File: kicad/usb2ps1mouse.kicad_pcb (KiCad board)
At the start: 2 copper layers, 42.7 x 35 mm, 11 parts, among them J1 Conn_01x09_Pin, J2 USB_A, U2 ME2108A50PG

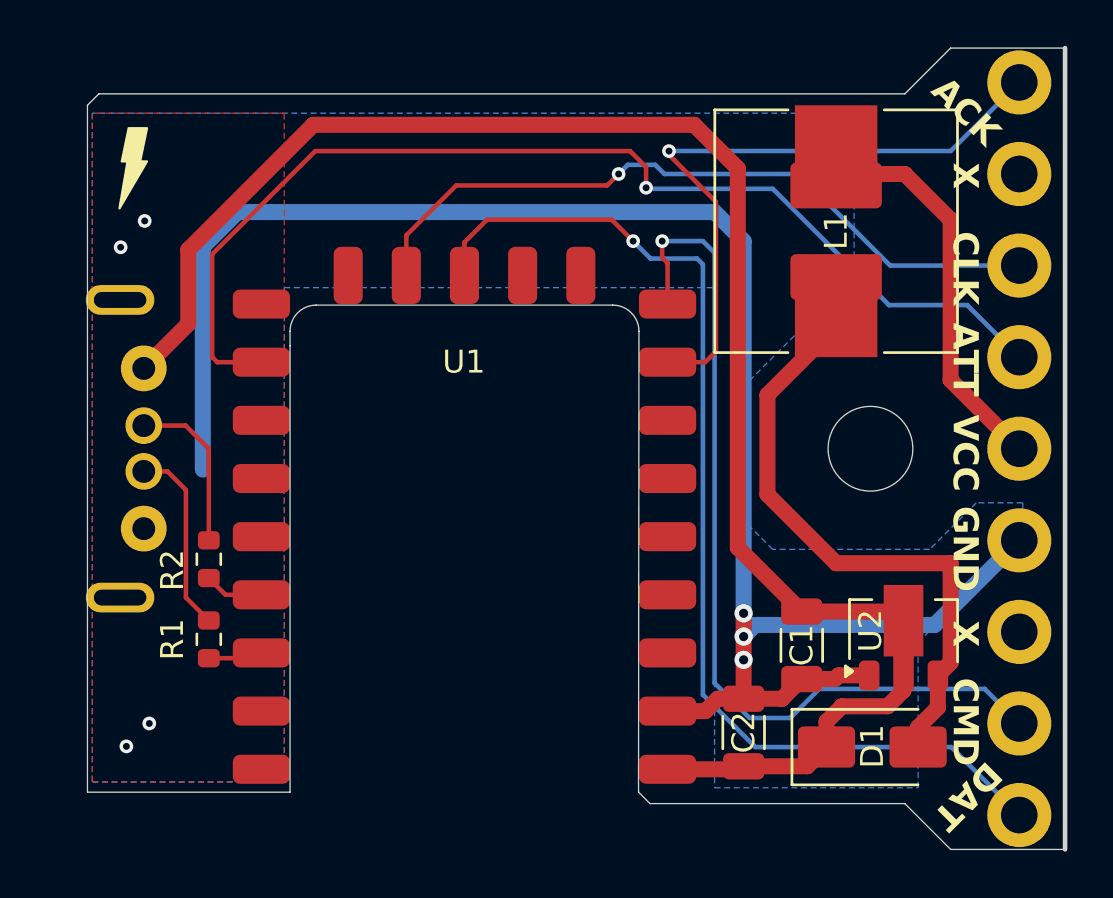
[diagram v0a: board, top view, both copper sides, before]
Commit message: Add PCB_3 board revision.
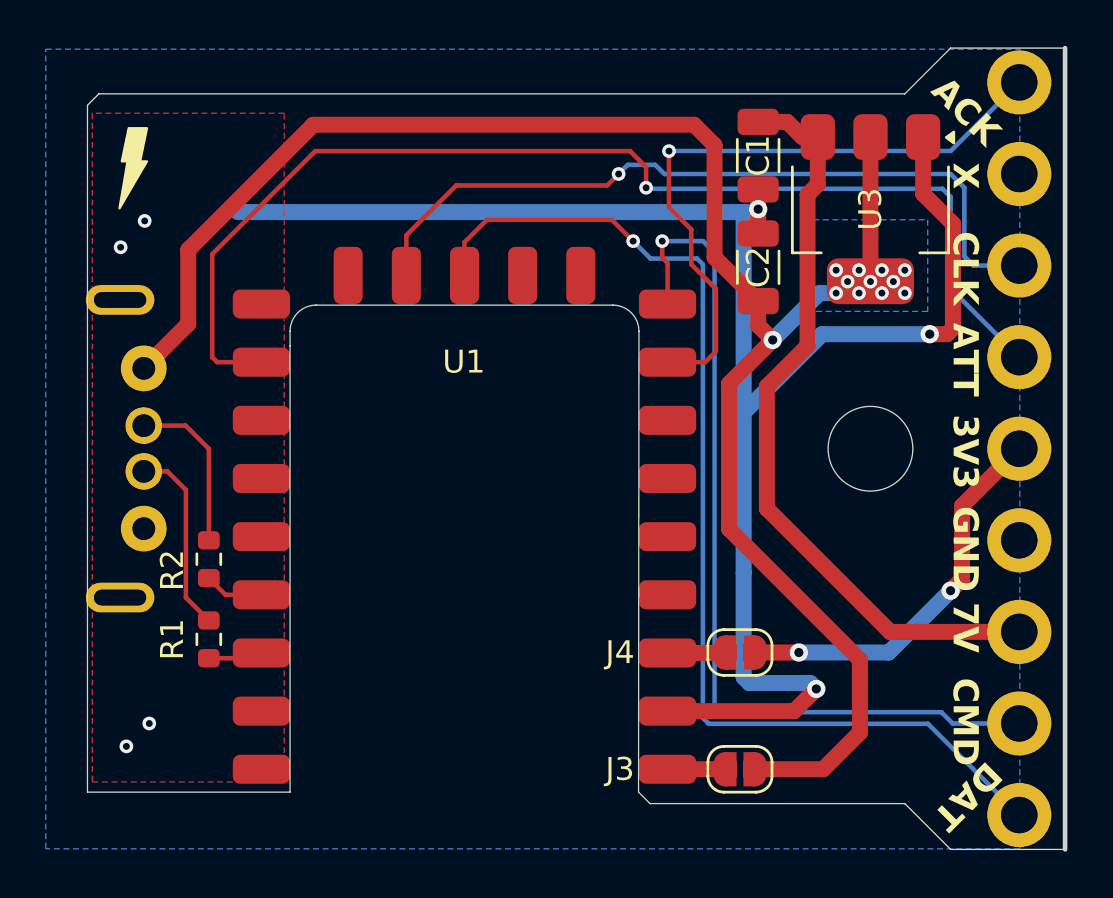
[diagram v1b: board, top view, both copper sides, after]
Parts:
- removed D1: SS14, Diode_SMD:D_SMA
- removed L1: 22u, usb2ps1mouse-specific:L_combo
- removed U2: ME2108A50PG, Package_TO_SOT_SMD:SOT-89-3
- added J3: Conn_01x02, Jumper:SolderJumper-2_P1.3mm_Open_RoundedPad1.0x1.5mm, F.Cu at (187.8, 114.0)
- added J4: Conn_01x02, Jumper:SolderJumper-2_P1.3mm_Open_RoundedPad1.0x1.5mm, F.Cu at (187.8, 108.9)
- added U3: AMS1117-5.0, Package_TO_SOT_SMD:SOT-223-3_TabPin2, F.Cu at (193.5, 89.5)
- U1: value ~ -> RP2040-Zero
- moved C1 21.5 mm to (188.6, 87.2)
- moved C2 20.3 mm to (188.6, 92.1)
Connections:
- C1 pad 1: +5V -> VMOT
- J1 pad 3: unconnected-(J1-Pin_3-Pad3) -> VMOT
- U1 pad 21: unconnected-(U1-3V3-Pad21) -> Net-(J4-Pin_2)
- U1 pad 23: +5V -> Net-(J3-Pin_2)
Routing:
- net VMOT: track 0.00 -> 33.3 mm
- net Net-(D1-A): track 26.5 -> 0.00 mm
- net GND: track 77.7 -> 75.0 mm
- net Net-(J4-Pin_2): track 0.00 -> 2.52 mm
- net Net-(J3-Pin_2): track 0.00 -> 2.51 mm
- net ATT: track 48.1 -> 50.5 mm
- net +5V: track 74.7 -> 76.6 mm, vias 0 -> 12
- net CLK: track 31.6 -> 33.4 mm
- net VCON: track 17.8 -> 17.1 mm, vias 0 -> 2
- net DATA: track 47.9 -> 48.5 mm
- added copper zone on B.Cu, net +5V
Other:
- board text added: "3V3"
- board text added: "7V"
- board text added: "PCB_3"
- board text removed: "PCB_2"
- board text removed: "VCC"
